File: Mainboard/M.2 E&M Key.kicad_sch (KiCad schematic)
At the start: 28 parts, among them J15 Bus_M.2_Socket_M, J16 Bus_M.2_Socket_E

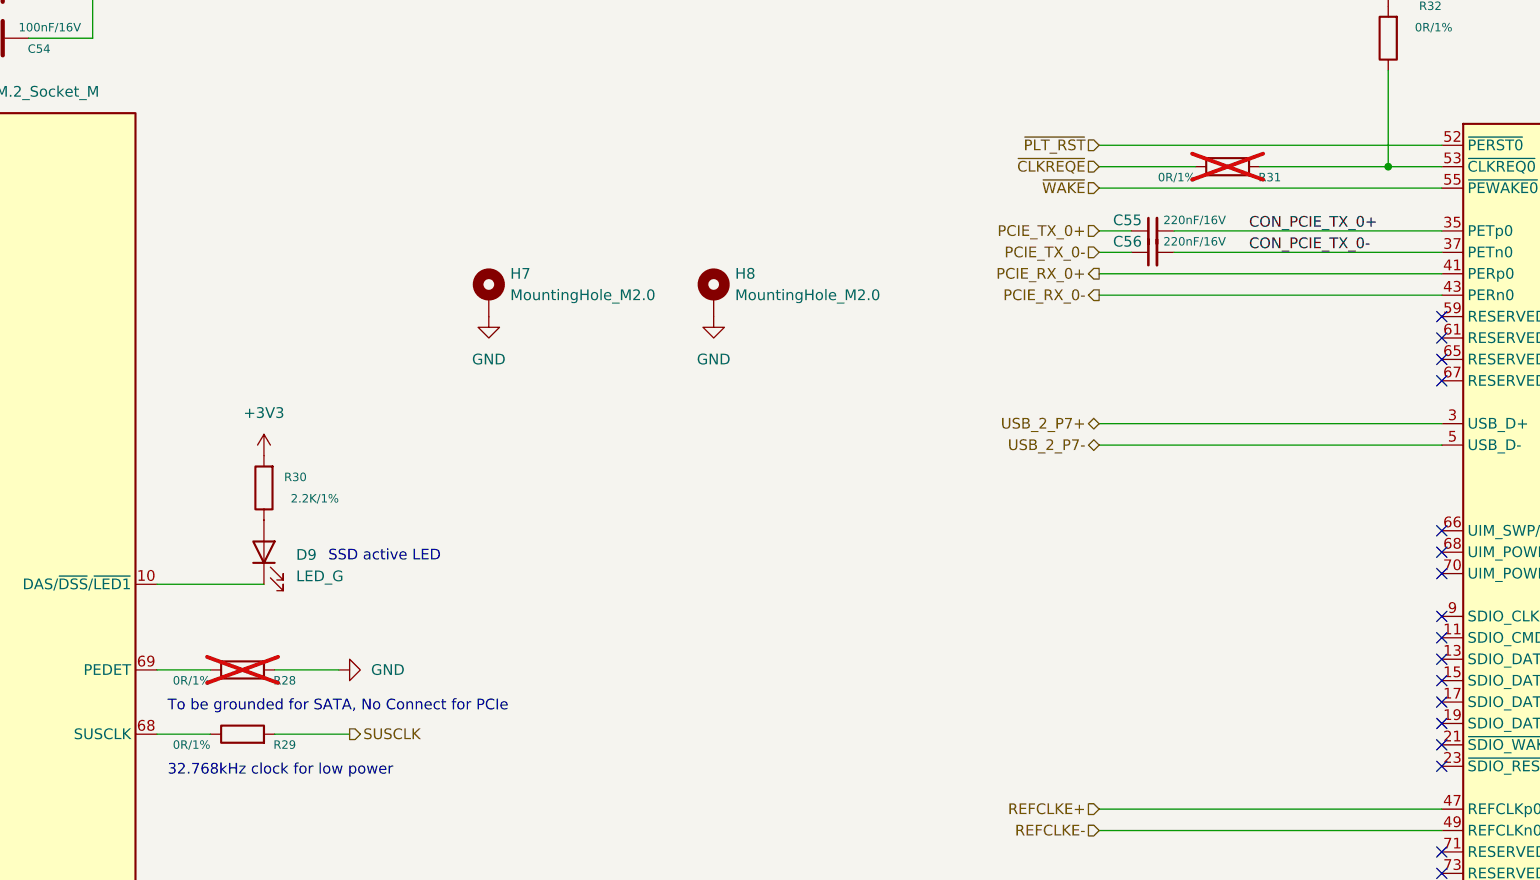
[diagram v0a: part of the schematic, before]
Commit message: Added HDMI > LDVS screens
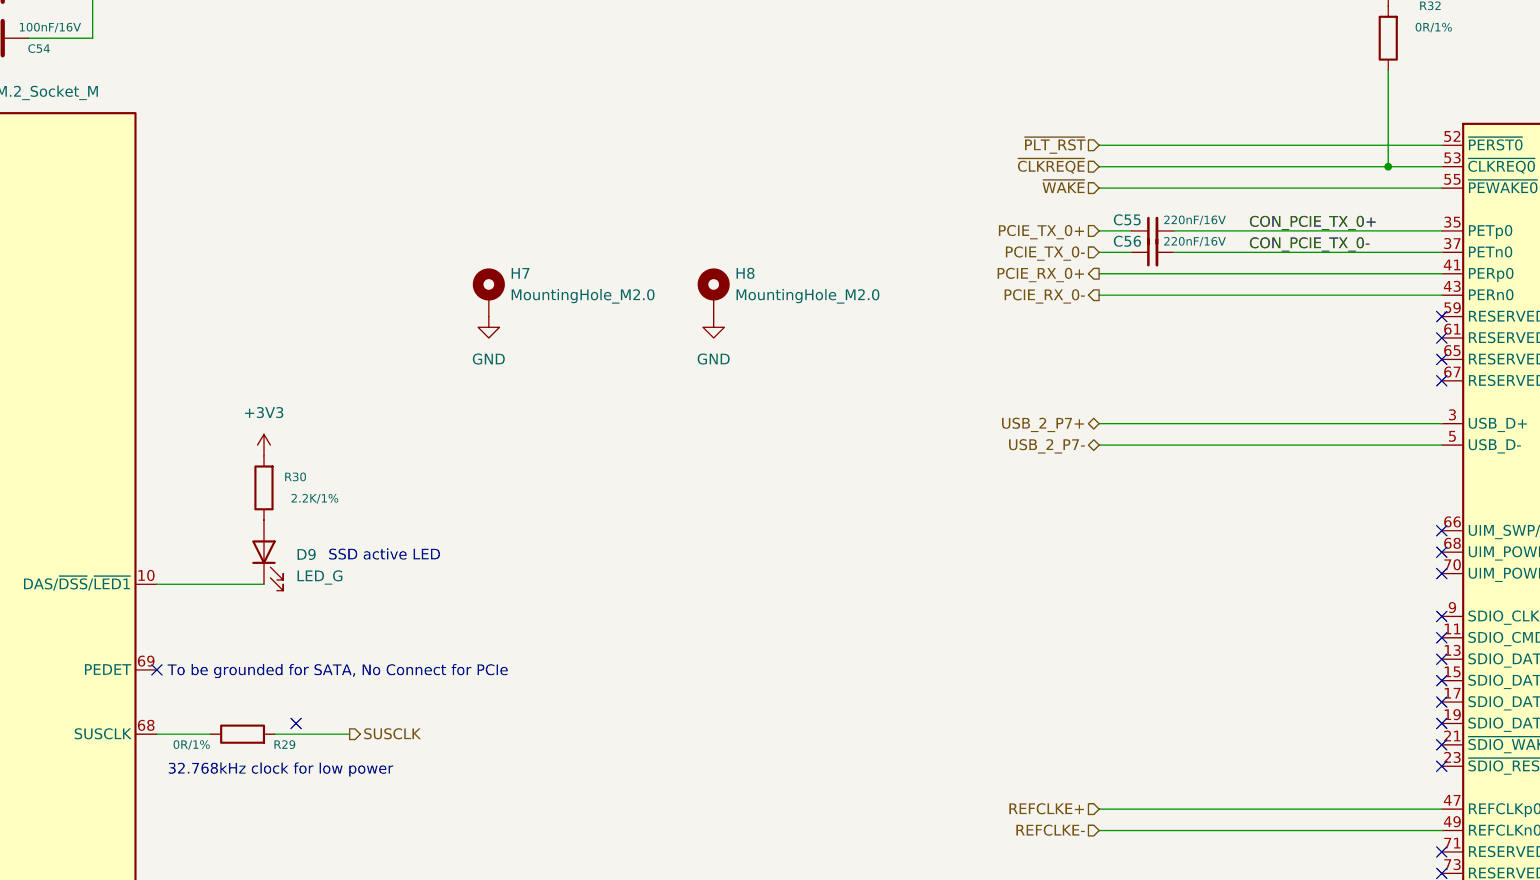
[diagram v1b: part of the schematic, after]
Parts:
- removed R28, R31: 0R/1%, A_HDJ_Library:R_0402_1005Metric, symbol Device:R
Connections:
- net ~{CLKREQE}: now also J16.53 (~{CLKREQ0}), R32.1
- no-connect marks 50 -> 52
